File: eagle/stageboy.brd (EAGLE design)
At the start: 120 x 75 mm, 38 parts, among them IC1 MEGA8-P, IC2 7805TV, J1 POWER_JACKPTH, Q1 16MHz, X1 MIDI IN, X2 MIDI OUT, X4 22-23-2021, X6 GBIO

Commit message: Picked a board layout and named it accordingly
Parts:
- removed R1, R2, R3: 10k, resistor:0204/7
- moved ISP 17.9 mm to (101.5, 28.2)
- moved R5 11.3 mm to (111.2, 29.5)
- moved R8 10.7 mm to (44.2, 11.5), turned to 90 degrees
- moved C1 8.50 mm to (80.0, 35.8)
- moved C2 7.75 mm to (98.5, 35.8)
- moved C3 7.25 mm to (76.2, 37.0)
- moved C4 7.25 mm to (76.2, 19.5)
- moved C9 7.25 mm to (95.0, 30.8)
- moved IC1 7.25 mm to (87.2, 33.2)
- moved Q1 7.25 mm to (76.2, 28.2)
- moved R10 4.80 mm to (21.0, 24.0), turned to 90 degrees
- moved OK1 3.13 mm to (36.5, 11.5)
- moved D1 2.80 mm to (27.8, 12.0)
- moved R9 2.57 mm to (24.2, 12.0)
- moved SW1 2.57 mm to (101.2, 19.2), turned to 90 degrees
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- renumbered JP2 to GB5V
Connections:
- removed net N$14: IC1.15, R2.2, SW1.2
- removed net N$15: IC1.16, R3.2, SW1.3
- new net N$5: IC1.15, SW1.5
- new net N$6: IC1.16, SW1.6
- net +5V: no longer SW1.4, SW1.5, SW1.6
- net GND: now also SW1.1, SW1.2, SW1.3; no longer R1.1, R2.1, R3.1
- net N$4: now also SW1.4; no longer R1.2, SW1.1
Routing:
- net N$23: track 46.0 -> 20.4 mm
- net N$25: track 38.2 -> 15.4 mm
- net N$15: track 22.4 -> 0.00 mm
- net N$35: track 77.8 -> 98.4 mm
- net N$14: track 18.9 -> 0.00 mm
- net N$11: track 92.0 -> 76.7 mm
- net N$5: track 0.00 -> 13.7 mm
- net N$18: track 32.4 -> 19.7 mm
- net N$32: track 42.8 -> 30.7 mm
- net N$17: track 25.3 -> 13.4 mm
- net N$4: track 24.1 -> 15.8 mm
- net N$26: track 18.7 -> 26.9 mm
- net N$6: track 0.00 -> 7.44 mm
- net N$27: track 16.9 -> 10.0 mm
- net N$1: track 40.1 -> 33.5 mm
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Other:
- outline, holes or cut-outs redrawn
- board text added: "5VDC!"
- board text added: "Thanks to SmashTV and Zunkworks for their awesome advice."
- board text removed: "10k"

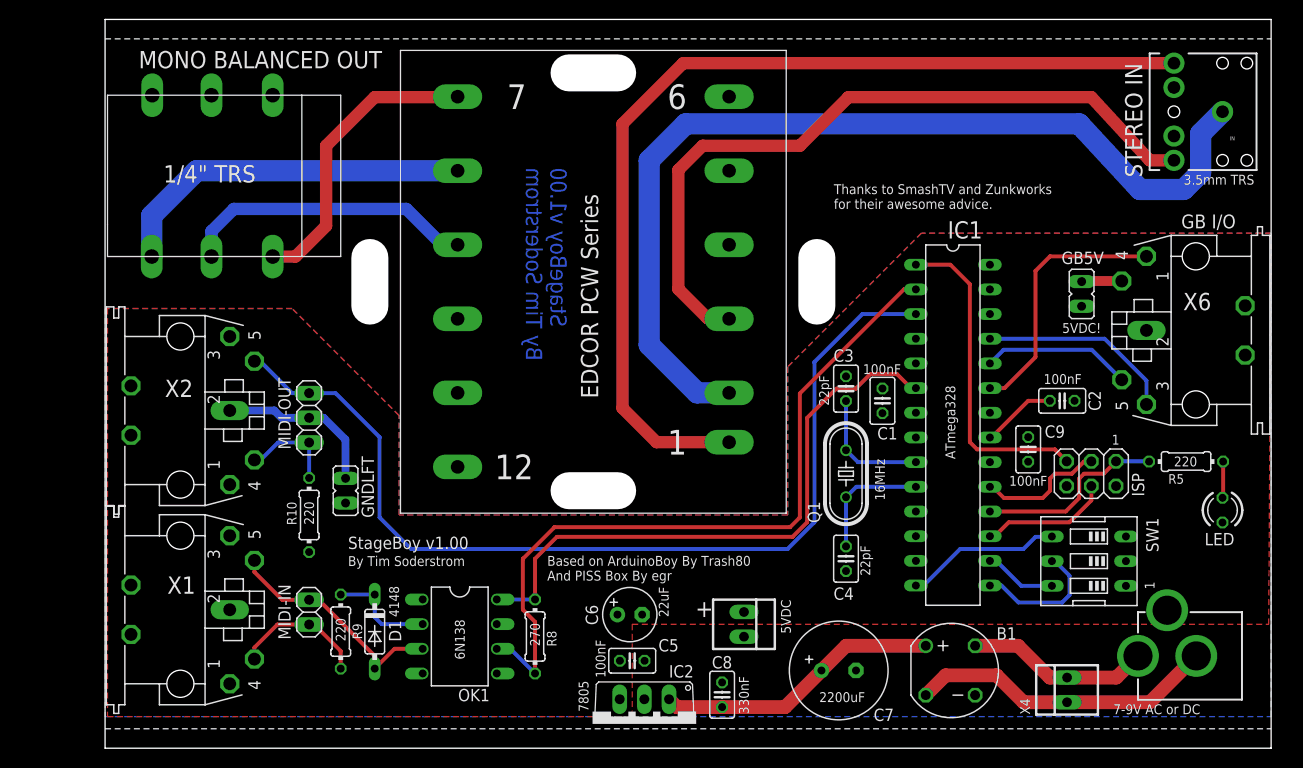
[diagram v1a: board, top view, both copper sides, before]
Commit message: Resized the electrolytic capacitors
The 2200uF cap was way too small, with the 22uF being only slightly
so. Both were changed and components shifted around as needed.
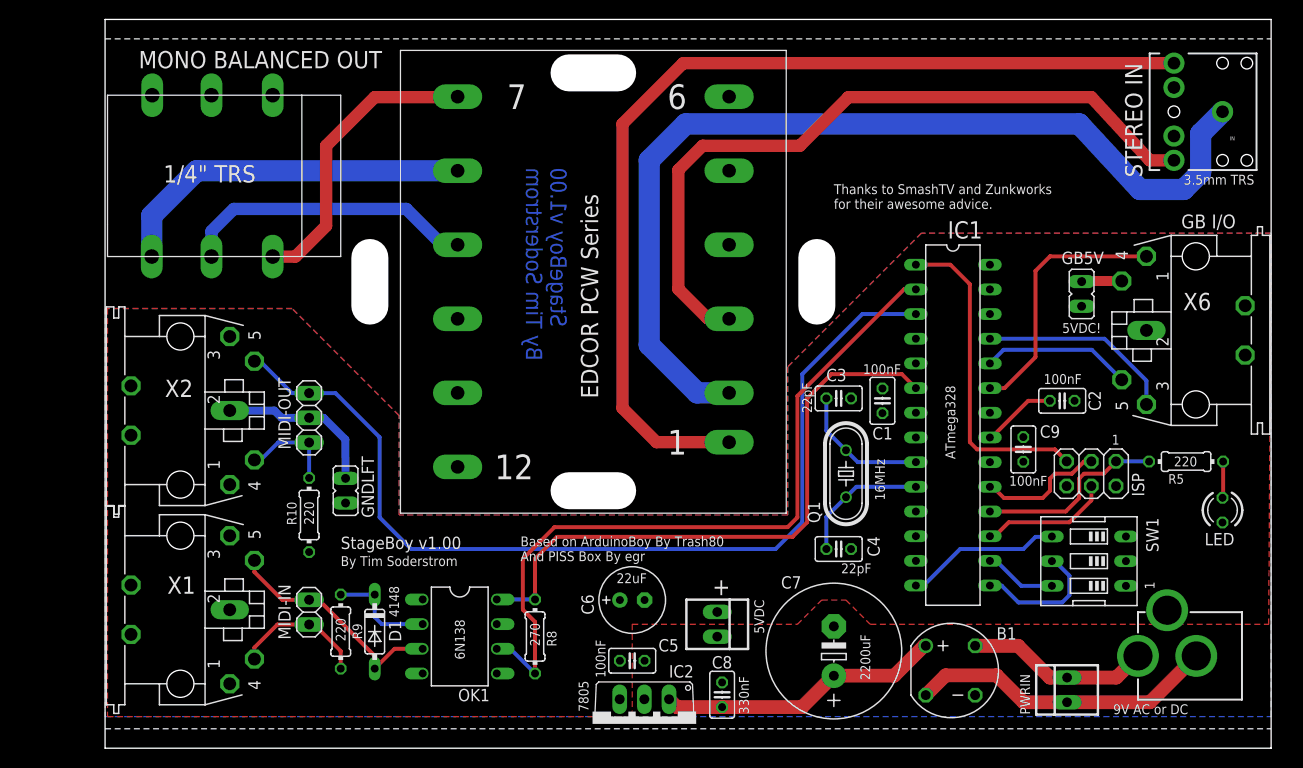
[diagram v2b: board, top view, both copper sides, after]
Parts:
- C6: device resistor:E2,5-6 -> resistor:E2,5-7
- C7: device resistor:E3,5-10 -> resistor:E5-13
- moved 5VDC 2.75 mm to (63.0, 12.8)
- moved C7 2.06 mm to (75.0, 10.0), turned to 90 degrees
- moved C6 1.52 mm to (54.2, 15.2)
- moved C3 1.25 mm to (75.5, 36.0), turned to 180 degrees
- moved C4 1.25 mm to (75.5, 20.5), turned to 180 degrees
- moved C9 0.50 mm to (94.5, 30.8)
- renumbered J1 to PWRJACK, X4 to PWRIN
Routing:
- net N$10: track 62.1 -> 63.3 mm
- net N$24: track 12.8 -> 13.9 mm
- net N$22: track 12.7 -> 13.8 mm
- net N$21: track 100.6 -> 99.9 mm
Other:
- board text added: "9V AC or DC"
- board text removed: "7-9V AC or DC"
